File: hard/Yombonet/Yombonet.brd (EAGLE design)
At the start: 83.8 x 49.2 mm, 28 parts, among them IC1 ATMEGA644-20PU, IC2 XC9572-PC44, IC3 LD1117, IC4 ESP-07ESP-07, Q3 16 MHz, X1 ZX-EDGE

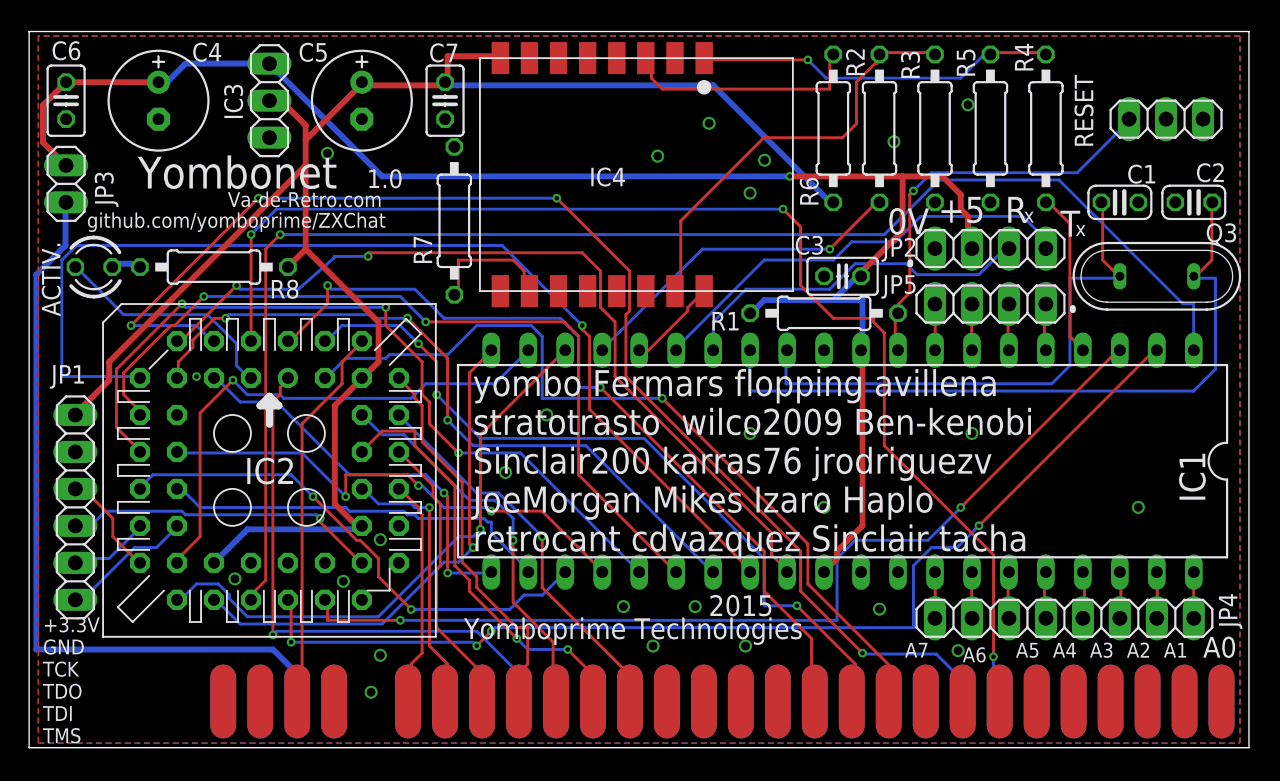
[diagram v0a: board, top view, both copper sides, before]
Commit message: Esquematico: Cambiados varios conectores a uno solo de 2x6
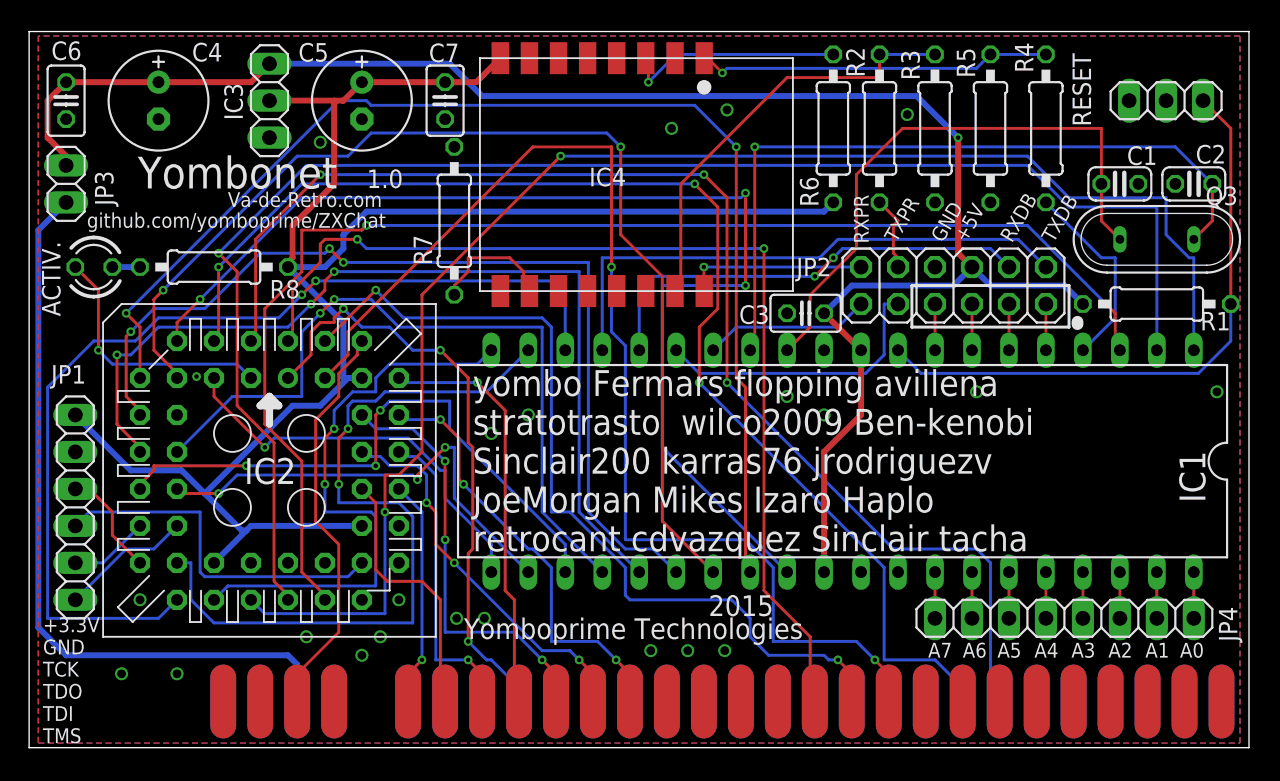
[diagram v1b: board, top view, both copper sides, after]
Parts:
- removed JP5: (no value), pinhead:1X04
- JP2: value PROG/COMM -> (none); device pinhead:1X04 -> pinhead:2X06
- moved R1 22.9 mm to (77.5, 30.5)
- moved JP2 3.59 mm to (63.5, 31.8), turned to 0 degrees
- moved C3 3.59 mm to (53.3, 29.8)
- moved Q3 2.54 mm to (77.5, 34.9)
- moved RESET 1.27 mm to (78.1, 44.5), turned to 180 degrees
- moved C1 1.27 mm to (74.9, 38.7)
- moved C2 1.27 mm to (80.0, 38.7)
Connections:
- new net RX0_5V_J: IC4.16, JP2.2
- new net TX0_5V_J: JP2.4, R2.2
- net +5V: now also JP2.8; no longer JP2.3
- net GND: now also IC2.25, IC2.27, IC2.28, IC2.29, JP2.6; no longer JP2.4
- net IO4: now also JP2.11; no longer JP5.1
- net IO5: now also JP2.9; no longer JP5.2
- net IO6: now also JP2.7; no longer JP5.3
- net IO7: now also JP2.5; no longer JP5.4
- net RX0_5V: now also JP2.1; no longer JP2.2
- net RX1_5V: now also JP2.10; no longer IC4.16
- net TX0_5V: now also JP2.3; no longer JP2.1
- net TX1_5V: now also JP2.12; no longer R2.2
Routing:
- net FLAG_WR1: track 73.5 -> 103.8 mm, vias 4 -> 1
- net RD_UC: track 39.6 -> 68.6 mm, vias 1 -> 2
- net BUSDATOSUC5: track 49.3 -> 75.1 mm, vias 3 -> 2
- net RX1_5V: track 6.33 -> 31.8 mm, vias 0 -> 2
- net WR_SINCLAIR: track 56.7 -> 81.4 mm, vias 1 -> 2
- net FLAG_WR0: track 66.1 -> 89.3 mm
- net BUSDATOSUC7: track 58.6 -> 79.3 mm, vias 2 -> 3
- net WR_UC: track 36.3 -> 53.1 mm, vias 1 -> 2
- net BUSDATOSUC2: track 34.8 -> 51.4 mm, vias 3 -> 2
- net TX1_5V: track 23.3 -> 38.1 mm, vias 1 -> 0
- net IORQ_SINCLAIR: track 56.5 -> 71.0 mm
- net RX0_5V: track 25.0 -> 11.5 mm
- net RESET_UC: track 28.5 -> 41.7 mm, vias 1 -> 0
- net RX0_5V_J: track 0.00 -> 12.4 mm, vias 0 -> 1
- net TX0_5V: track 30.5 -> 19.9 mm
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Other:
- board text added: "+5V"
- board text added: "GND"
- board text added: "RXDB"
- board text added: "RXPR"
- board text added: "TXDB"
- board text added: "TXPR"
- board text removed: "+5"
- board text removed: "0V"
- board text removed: "R"
- board text removed: "T"
- board text removed: "x"

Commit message: PCB: Cambios en pistas, serigrafia y posicion vias
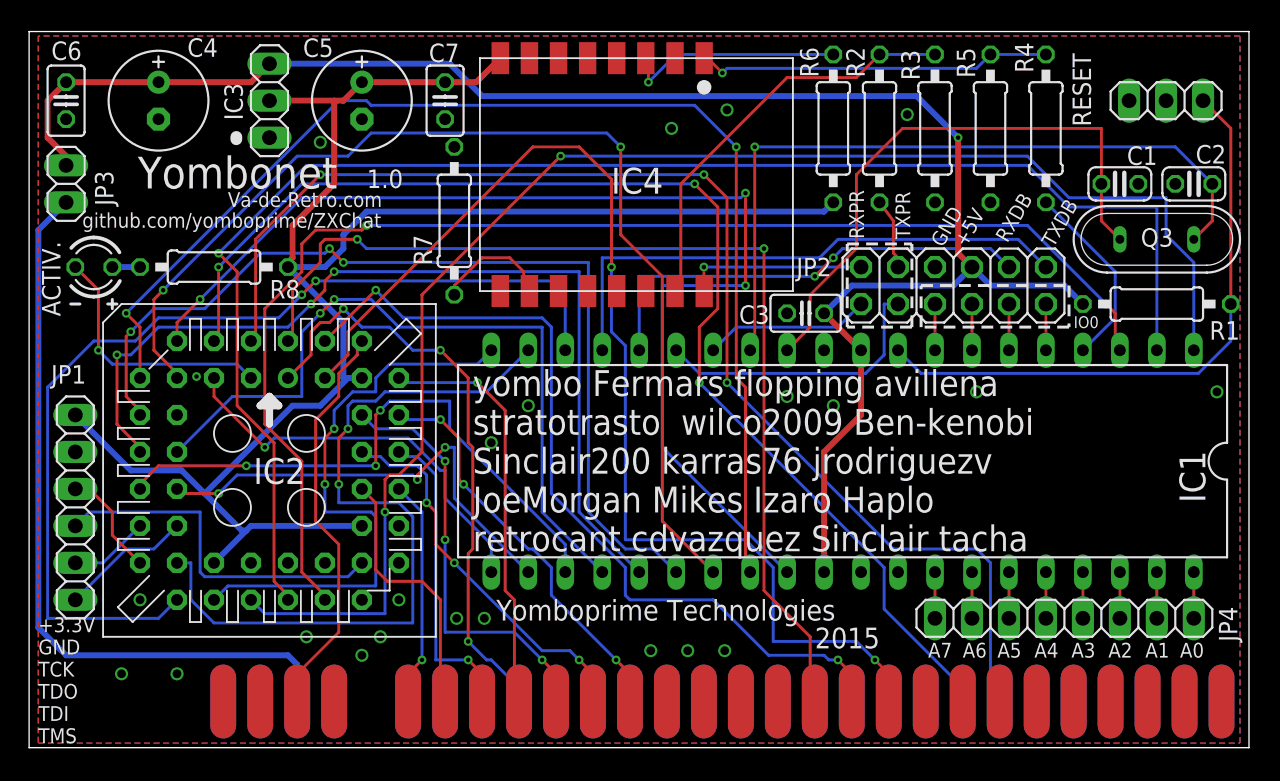
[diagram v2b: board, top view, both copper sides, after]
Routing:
- net ADDR_SINCLAIR2: track 86.6 -> 84.5 mm
- net BUSDATOSSINCLAIR4: track 29.8 -> 27.9 mm
- net RD_SINCLAIR: track 59.8 -> 58.3 mm
- net WR_SINCLAIR: track 81.4 -> 80.1 mm
- net N$1: track 29.6 -> 28.7 mm
- net RST_WIFI: track 13.6 -> 13.1 mm
- net GPIO15_PULLDOWN: track 8.64 -> 8.08 mm
- net FLAG_WR0: track 89.3 -> 88.8 mm
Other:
- board text added: "IO0"
